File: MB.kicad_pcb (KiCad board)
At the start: 4 copper layers, 90.2 x 94.1 mm, 51 parts, among them J100 VCC INPUT, J101 SWITCH ON/OFF, J103 FAN VOLTAGE, J200 DOOR_OUTPUT, J300 MCP_EXTERNAL, J301 CAN_INPUT, K200 HF49FD/005-1H12T, Q100 WST4045, Q200 MMBT3904, U100 LM2596S-5, U101 AMS1117-3.3, U200 MEGA_PRO_EMBED_CH340G_{slash}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, U300 MCP2515-xSO, U301 TJA1051T-3, Y300 8MHz

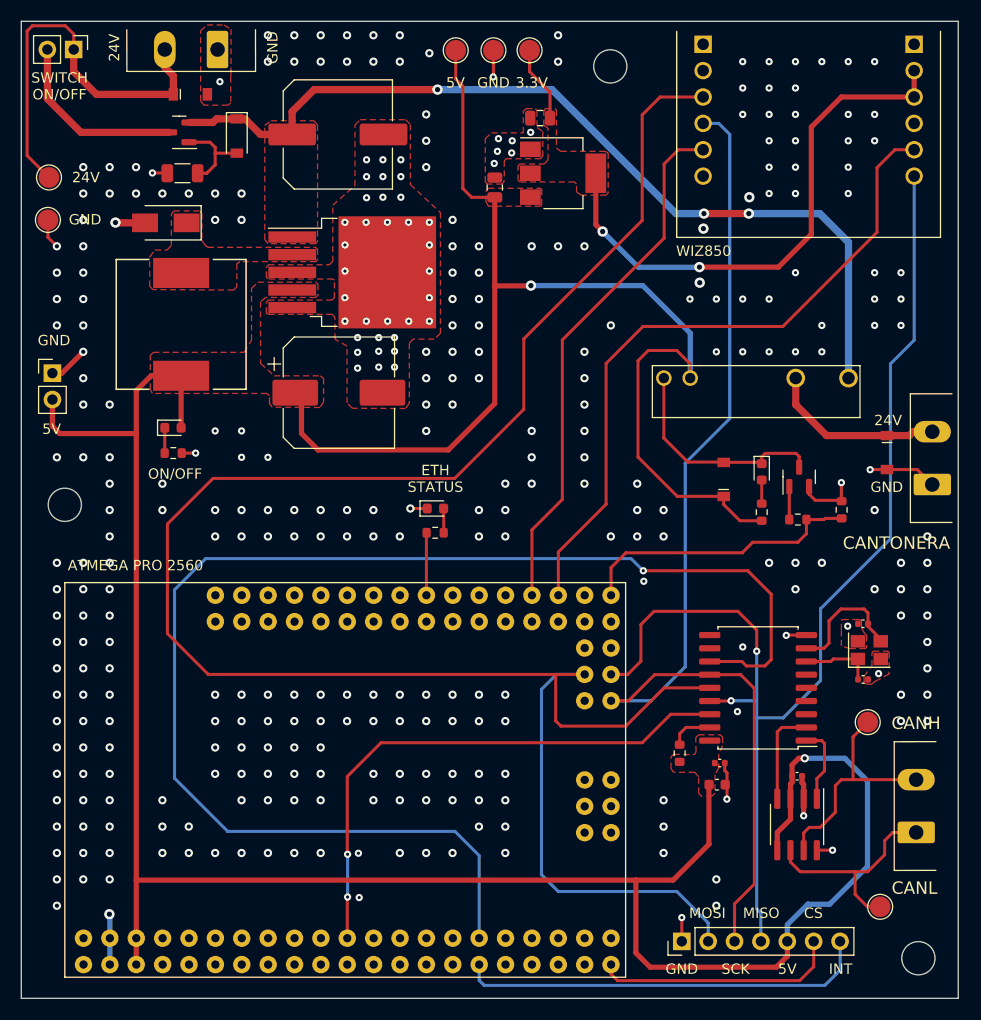
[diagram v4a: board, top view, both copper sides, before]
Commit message: move position of arduino mega and wiz850
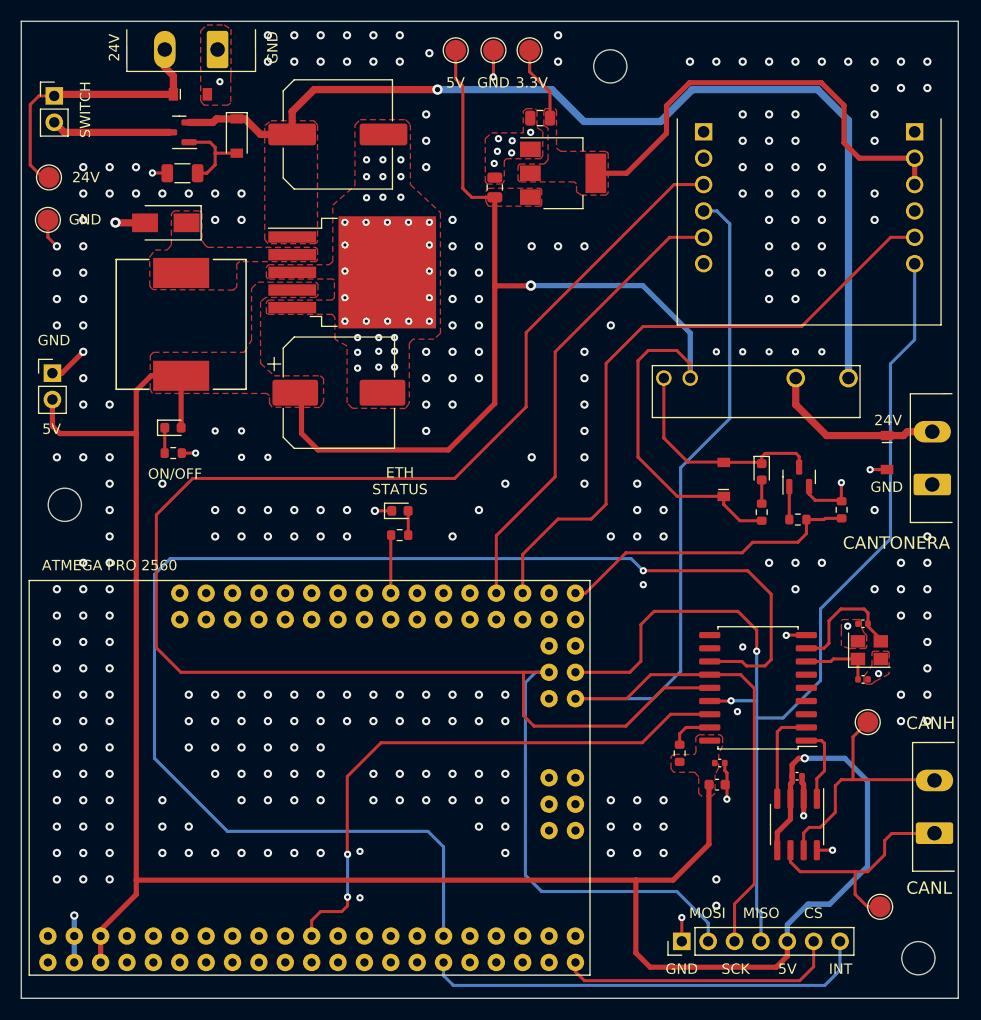
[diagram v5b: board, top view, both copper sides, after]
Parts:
- moved H200 8.43 mm to (204.2, 44.5)
- moved J101 4.85 mm to (131.8, 36.3), turned to 0 degrees
- moved U200 3.44 mm to (156.4, 102.0)
- moved R200 3.42 mm to (165.1, 78.6)
- moved D200 3.42 mm to (165.1, 76.3)
- moved J301 1.77 mm to (216.6, 107.3)
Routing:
- net /POWER/V_INPUT: track 38.8 -> 27.0 mm
- net +24V: track 86.5 -> 95.9 mm, vias 3 -> 1
- net +3V3: track 60.0 -> 50.9 mm, vias 2 -> 0
- net ETH_CS: track 51.1 -> 44.5 mm
- net Net-(J101-Pad2): track 17.9 -> 11.5 mm
- net SPI_MOSI: track 194.3 -> 188.2 mm
- net GND: track 47.0 -> 41.7 mm, vias 347 -> 346
- net SPI_MISO: track 114.0 -> 108.9 mm
- net ETH_RST: track 66.1 -> 62.1 mm
- net CS_EXT: track 23.7 -> 27.2 mm
- net INT_EXT: track 39.9 -> 43.2 mm
- net CS_CAN: track 53.0 -> 55.4 mm
- net SPI_SCK: track 105.1 -> 103.2 mm
- net /CAN/CANH: track 22.3 -> 24.0 mm
- net /MCU/PRINCIPAL_DOOR: track 27.6 -> 29.4 mm
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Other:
- board text added: "SWITCH"
- board text removed: "SWITCH ON/OFF"
- board text removed: "WIZ850"

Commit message: added logo
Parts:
- added G***: LOGO, LOGO, F.Cu at (179.3, 63.7)

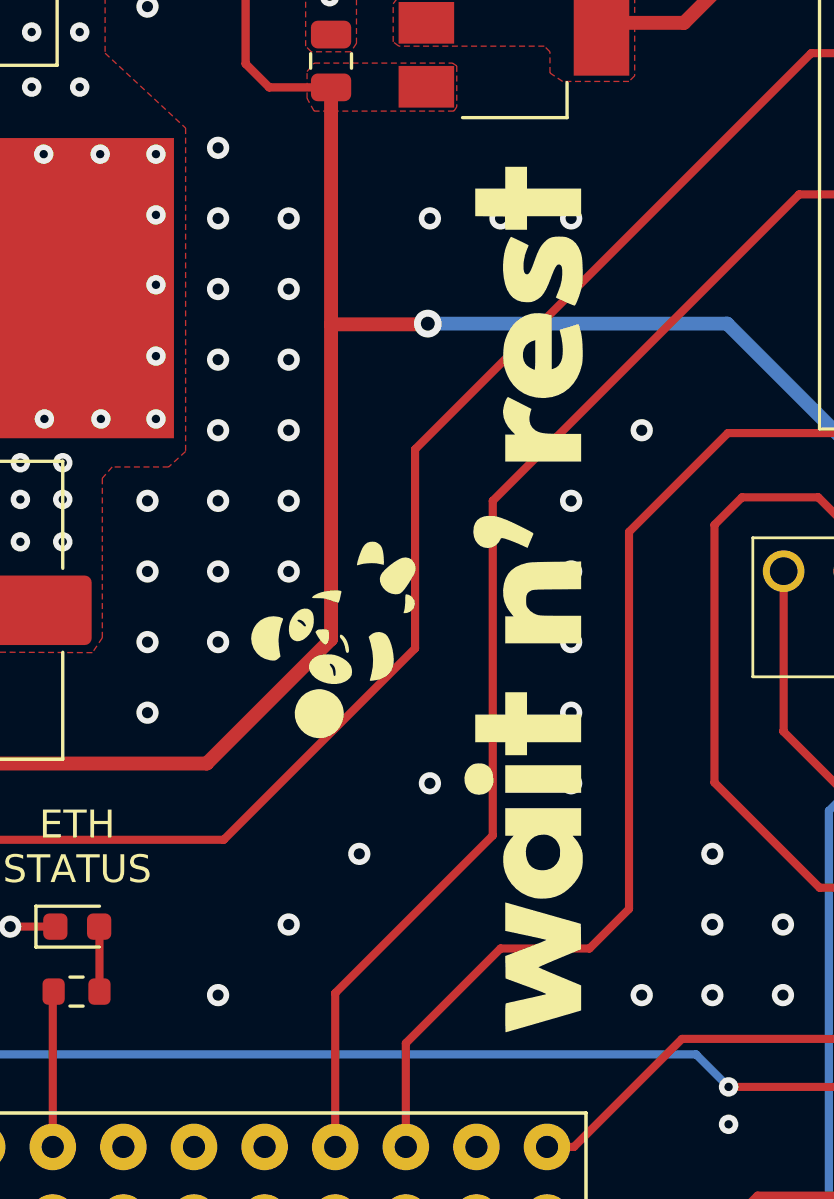
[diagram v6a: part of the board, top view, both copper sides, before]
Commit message: change board stackup and logo
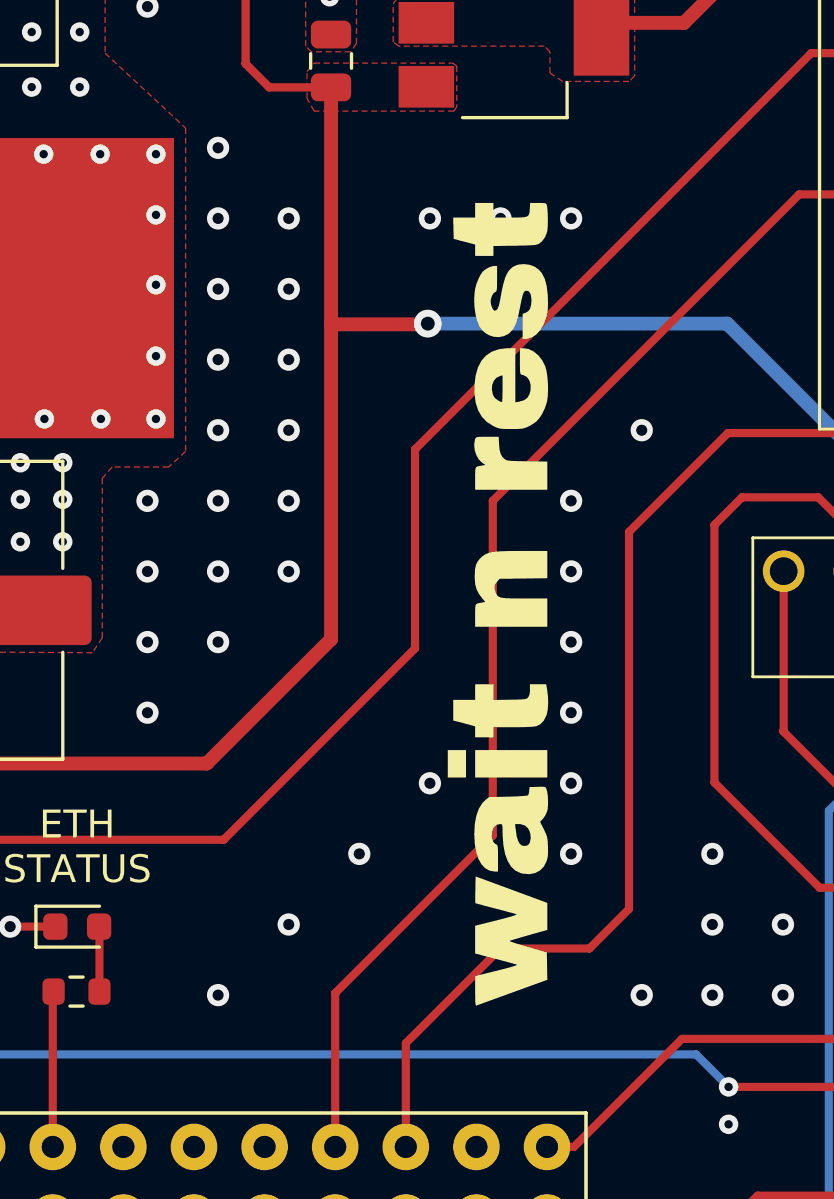
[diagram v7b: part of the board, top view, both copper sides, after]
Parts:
- moved G*** 1.38 mm to (180.3, 64.7)
